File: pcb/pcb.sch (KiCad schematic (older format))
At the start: 64 parts, among them J1 TYPE-C-31-M-12, J2 AudioJack4, J3 AudioJack4, SW1 SW_Push, SW10 SW_Push, SW11 SW_Push, SW12 SW_Push, SW13 SW_Push, SW14 SW_Push, SW15 SW_Push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

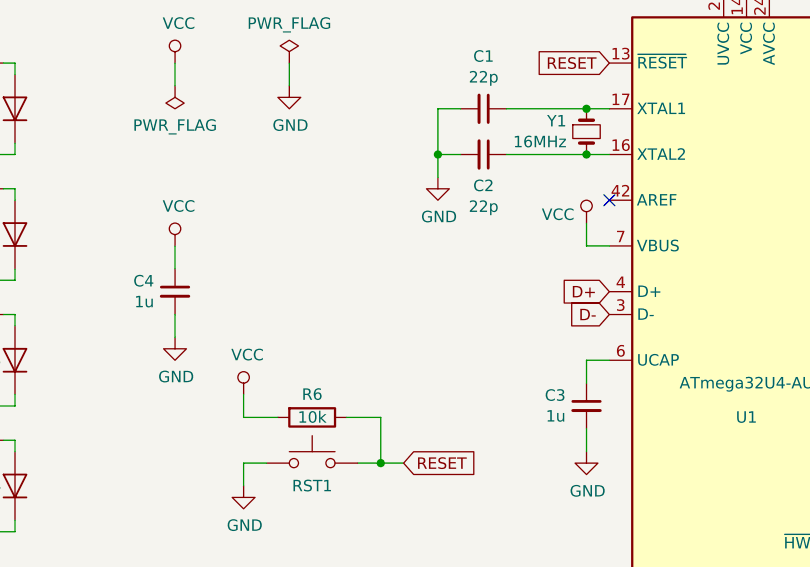
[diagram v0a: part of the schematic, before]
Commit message: + I2C pullup
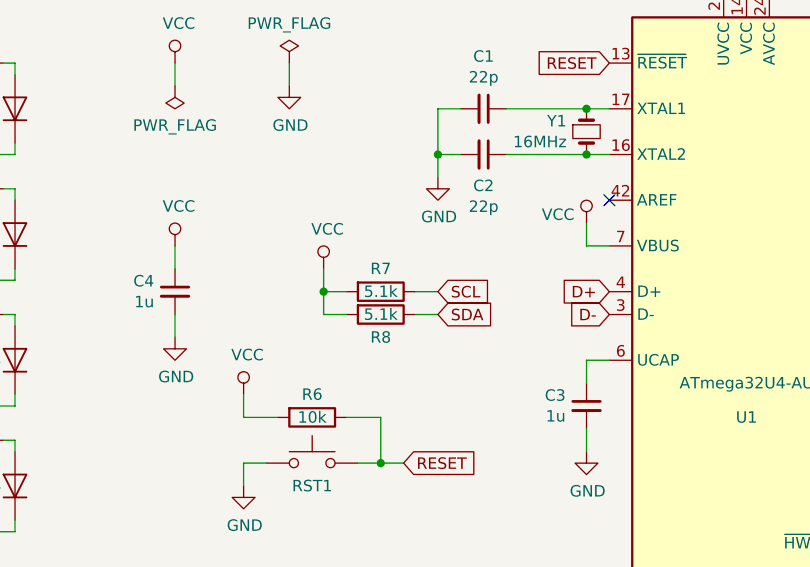
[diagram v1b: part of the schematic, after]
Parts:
- added R7, R8: 5.1k, SMD:2012M, symbol Device:R
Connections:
- net SCL: now also R7.1
- net SDA: now also R8.1
- net VCC: now also R7.2, R8.2
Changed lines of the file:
@@
 NoConn ~ 9600 1700
 NoConn ~ 9600 1800
+Text GLabel 7650 2600 2    50   Input ~ 0
+SDA
+Text GLabel 7650 2500 2    50   Input ~ 0
+SCL
+$Comp
+L Device:R R7
+U 1 1 5F46E4EC
+P 7400 2500
+F 0 "R7" V 7300 2500 50  0000 C CNN
+F 1 "5.1k" V 7400 2500 50  0000 C CNN
+F 2 "SMD:2012M" V 7330 2500 50  0001 C CNN
+F 3 "~" H 7400 2500 50  0001 C CNN
+	1    7400 2500
+	0    1    1    0
+$EndComp
+$Comp
+L Device:R R8
+U 1 1 5F46EF19
+P 7400 2600
+F 0 "R8" V 7500 2600 50  0000 C CNN
+F 1 "5.1k" V 7400 2600 50  0000 C CNN
+F 2 "SMD:2012M" V 7330 2600 50  0001 C CNN
+F 3 "~" H 7400 2600 50  0001 C CNN
+	1    7400 2600
+	0    1    1    0
+$EndComp
+Wire Wire Line
+	7550 2500 7650 2500
+Wire Wire Line
+	7550 2600 7650 2600
+Wire Wire Line
+	7250 2500 7150 2500
+Wire Wire Line
+	7150 2500 7150 2400
+Wire Wire Line
+	7250 2600 7150 2600
+Wire Wire Line
+	7150 2600 7150 2500
+Connection ~ 7150 2500
+$Comp
+L power:VCC #PWR0103
+U 1 1 5F4997B4
+P 7150 2400
+F 0 "#PWR0103" H 7150 2250 50  0001 C CNN
+F 1 "VCC" H 7167 2573 50  0000 C CNN
+F 2 "" H 7150 2400 50  0001 C CNN
+F 3 "" H 7150 2400 50  0001 C CNN
+	1    7150 2400
+	1    0    0    -1
+$EndComp
 $EndSCHEMATC
